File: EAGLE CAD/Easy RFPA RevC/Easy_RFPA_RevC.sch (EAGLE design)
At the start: 305 parts, among them IC1 LM741D, IC2 LM741D, IC3 LM393D, IC5 74AHC1G00DBV, IC6 74LS74D, IC7 74AHC1G86DBV, J101 COAX112640BNC_EDGE, J102 COAX112640BNC_EDGE, J301 COAX112640BNC_EDGE, J302 COAX112640BNC_EDGE, J401 HDR_2X1282836-1282836-1, J402 KK_PCFAN, Q1 IRF630, Q101 IRF520N, Q102 IRF630, Q2 MOSFET_NBSS123SOT23, Q201 IRF630, Q202 IRF630, Q3 NPNMMBT3904SOT23_BEC, Q301 MOSFET_NBSS123SOT23, Q302 PNPSOT23_BEC, Q303 NPNMMBT3904SOT23_BEC, Q4 PNPSOT23_BEC, T1 HP1_TRAFO, T102 HP4_TRAFO, U1 OPAMP_QUADTLV274IDSOIC14, U302 OPAMP_QUADTLV274IDSOIC14, U401 LDO_3TERMMC78M12CTGTO220_VERT, U402 LDO_3TERMMC78M05CTGTO220_VERT, X1 1-227161-0, X2 1-227161-0, X3 1-227161-0, X4 1-227161-0, X402 HEATSINK_OMNI_DUALOMNI-UNI-30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

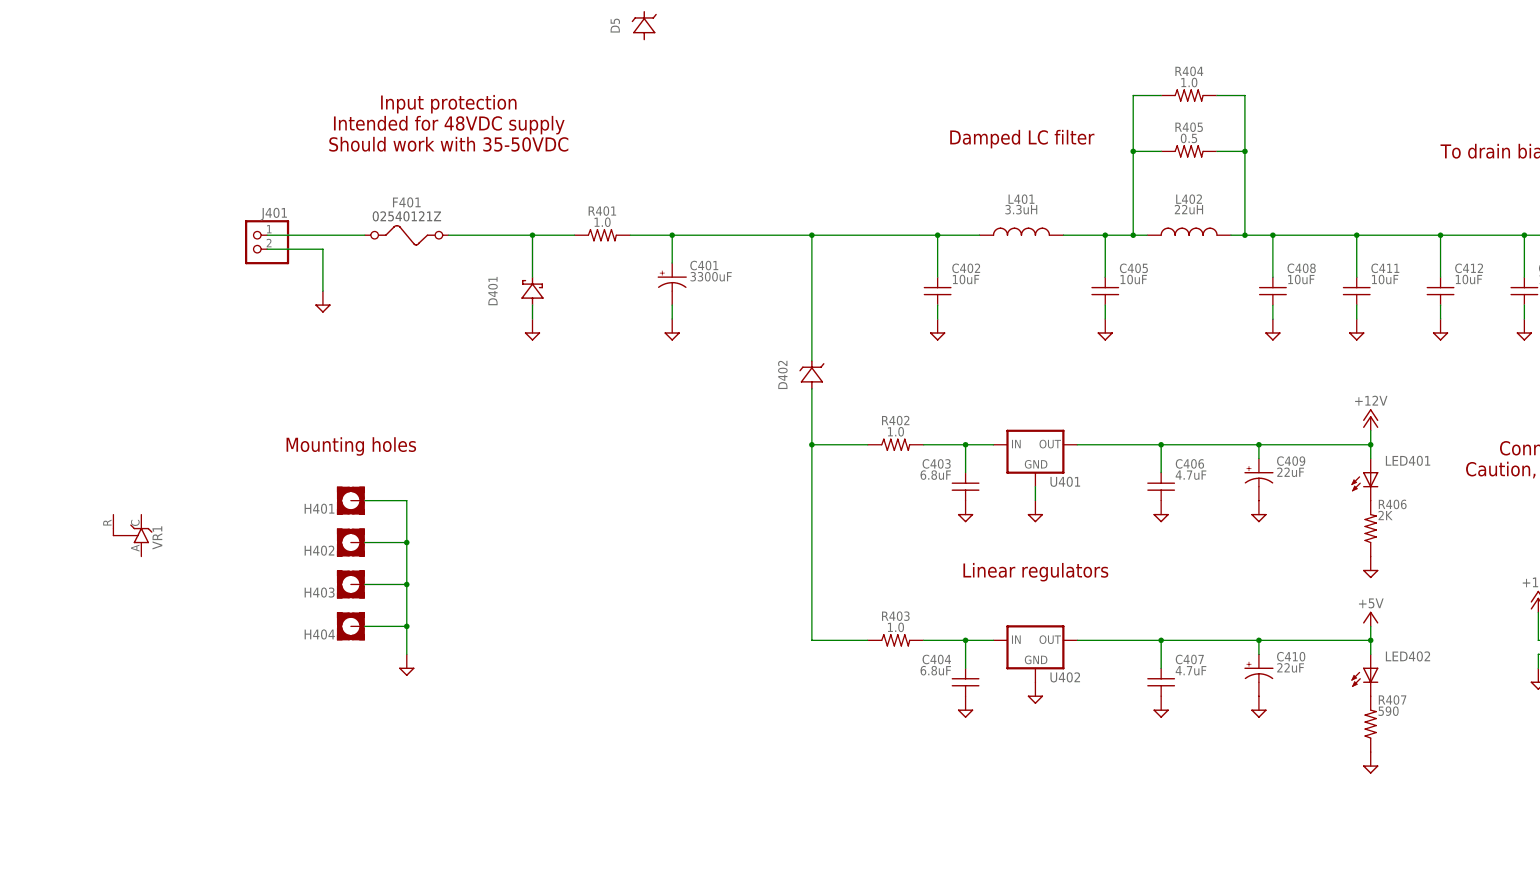
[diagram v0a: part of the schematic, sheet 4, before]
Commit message: Move connectors/LEDs/buttons to west edge
Aiming to have these poke through a panel.
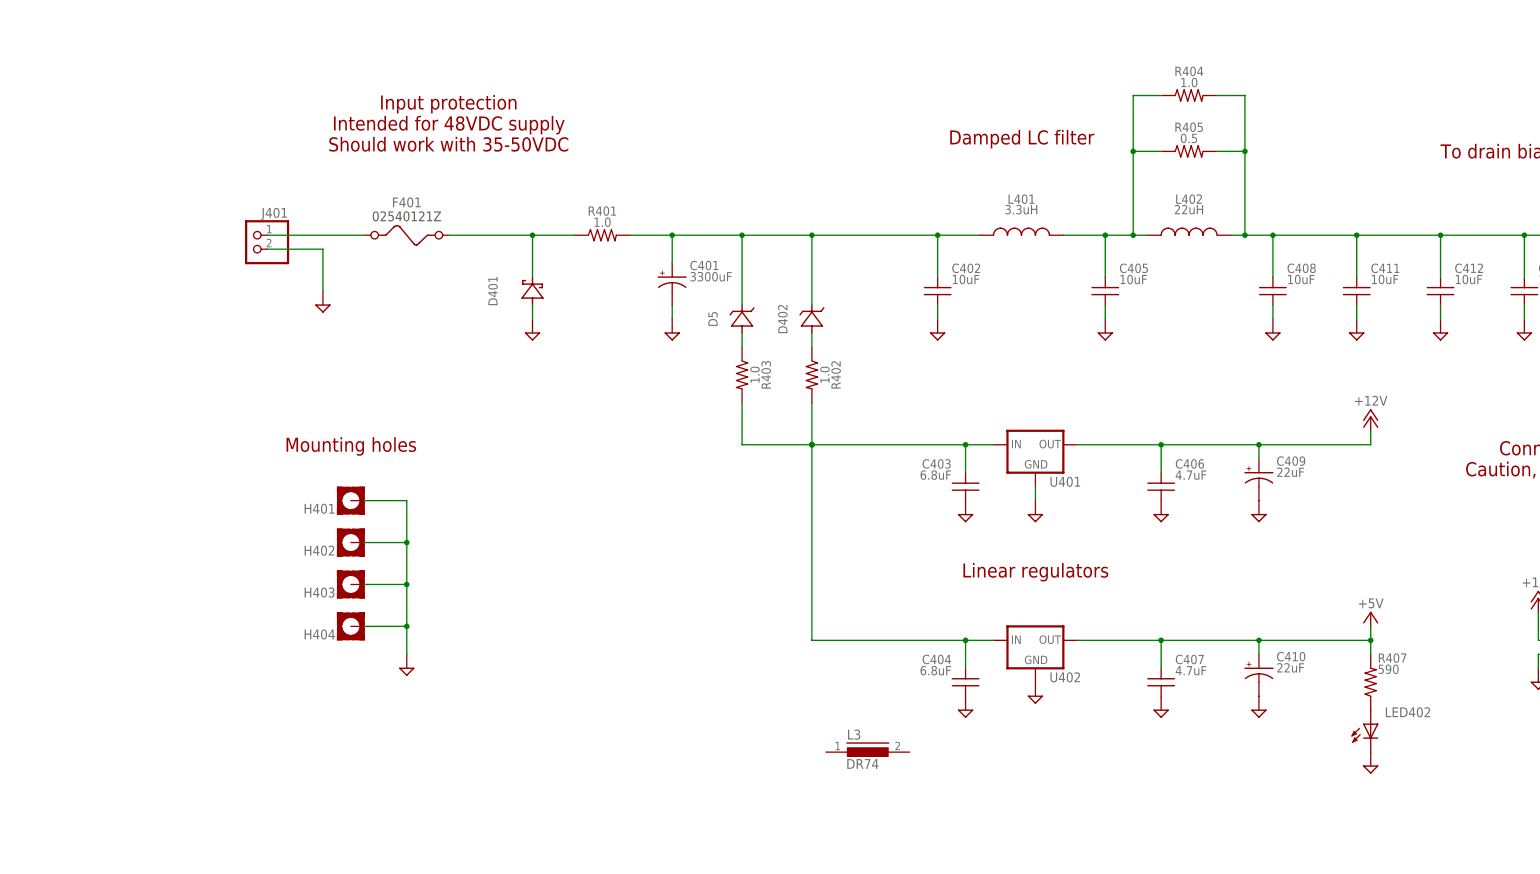
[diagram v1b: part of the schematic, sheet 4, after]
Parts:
- removed C114, C115, C211, C212: 10nF, MDT_C:CGEN0805_IPC
- removed J101, J102, J301, J302: COAX112640BNC_EDGE, MDT_CON:COAX112640BNC_EDGE
- removed LED401: LEDHLMP-3962-F0002T1_3/4, MDT_Diode:LEDHLMP-3962-F0002T1_3/4
- removed R130, R131, R229, R230, R24: 1K, MDT_R:R90GEN0805_IPC
- removed R406: 2K, MDT_R:RGEN0805_IPC
- removed S1, S2: (no value), switch-omron:10-XX
- removed TP14, TP15, TP16, TP17, TP24: PROBE_TPTP_5MM, MDT_CON:PROBE_TPTP_5MM
- removed VR1: (no value), v-reg:TL431CLP
- added L1: (no value), MDT_L:LDR74
- added L3: DR74, inductors:DR74
- added SW1, SW2: SPST_NO_TACT_RA431256083716431256083716, MDT_SWITCH:SPST_NO_TACT_RA431256083716431256083716
- C8: value 10nF -> 22nF; device MDT_C:CGEN0805_IPC -> MDT_C:CC-22N-250V-5%-1206-NP0C1206; BOM (none) -> EXCLUDE; VOLTAGE 50V -> (none)
- LED1, LED2: value LEDHLMP-3401-E0002T1_3/4 -> LEDT1_3/4_RA; device MDT_Diode:LEDHLMP-3401-E0002T1_3/4 -> MDT_Diode:LEDT1_3/4_RA
- LED402: value LEDHLMP-3962-F0002T1_3/4 -> LEDT1_3/4_RA; device MDT_Diode:LEDHLMP-3962-F0002T1_3/4 -> MDT_Diode:LEDT1_3/4_RA
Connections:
- removed net AN6: C115.1, R131.2, TP15.1
- removed net AP6: C114.1, R130.2, TP14.1
- removed net BN6: C212.1, R230.2, TP17.1
- removed net BP6: C211.1, R229.2, TP16.1
- removed net N$49: C404.1, R403.2, U402.IN
- removed net S1_BP6: C8.1, R24.2, TP24.1
- net !FAULT: now also SW1.P1; no longer S2.P, S2.P1
- net +12V: no longer LED401.A
- net +5V: now also R407.1, SW2.P1; no longer LED402.A, S1.P, S1.P1
- net AN5: no longer R131.1
- net AP5: no longer R130.1
- net BN5: no longer R230.1
- net BP5: no longer R229.1
- net GND: now also LED402.C, SW1.G1, SW1.G2, SW1.S1, SW2.G1, SW2.G2; no longer C114.2, C115.2, C211.2, C212.2, C8.2, J101.GND1, J102.GND1, J302.GND1, R406.2, R407.2, S2.S, S2.S1, TP14.GND1, TP15.GND1, TP16.GND1, TP17.GND1, TP24.GND1
- net N$20: no longer J301.1
- net N$21: no longer J301.GND1
- net N$28: now also D5.A1; no longer D402.A1, R402.1
- net N$31: no longer J102.1
- net N$32: now also D402.A1, R402.1; no longer LED401.C, R406.1
- net N$33: now also LED402.A, R407.2; no longer LED402.C, R407.1
- net N$43: now also C404.1, R403.2, U402.IN
- net N$46: now also D5.C1
- net N$53: no longer J302.1
- net N$69: no longer J101.1
- net RESET: now also SW2.S1; no longer S1.S, S1.S1
- net S1_BP5: no longer R24.1
- net S2_DP: now also C8.2, L1.1
- net VB: now also C8.1, L1.2
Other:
- moved on the sheet: C4, C8, D402, D5, LED402, R402, R403, R407, R8

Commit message: Try and keep area under 30 square inches
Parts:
- removed L3: DR74, inductors:DR74
- removed X3: 1-227161-0, con-coax:1-227161-0
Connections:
- net N$20: no longer X3.1
- net N$21: no longer X3.2
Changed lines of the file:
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@@
 <part name="X1" library="con-coax" deviceset="?227161*" device="1-" technology="-0"/>
 <part name="X2" library="con-coax" deviceset="?227161*" device="1-" technology="-0"/>
-<part name="X3" library="con-coax" deviceset="?227161*" device="1-" technology="-0"/>
 <part name="X4" library="con-coax" deviceset="?227161*" device="1-" technology="-0"/>
 <part name="SUPPLY6" library="supply2" deviceset="GND" device=""/>
@@
 <variant name="IRF630_200W"/>
 </part>
-<part name="L3" library="inductors" deviceset="DR74" device=""/>
 <part name="C8" library="MDT_C" deviceset="C" device="C1206" technology="C-22N-250V-5%-1206-NP0" value="22nF">
 <attribute name="BOM" value="EXCLUDE"/>
 </part>
 <part name="D5" library="MDT_Diode" deviceset="D-ZENER" device="DO15-12" technology="1N5355B-TP" value="D-ZENER1N5355B-TPDO15-12"/>
+<part name="X3" library="MDT_HEATSINK" deviceset="THERMALPAD_TO220" device="" technology="DC0011/15-TI900-0.12-0"/>
+<part name="X5" library="MDT_HEATSINK" deviceset="HEATSINK_CLIP" device="" technology="OMNI-220C"/>
 </parts>
 <sheets>
@@
 <instance part="U1" gate="C" x="111.76" y="83.82"/>
 <instance part="U1" gate="P" x="200.66" y="76.2"/>
-<instance part="X3" gate="G$1" x="66.04" y="246.38"/>
 <instance part="SUPPLY42" gate="GND" x="93.98" y="78.74" smashed="yes"/>
 <instance part="R44" gate="G$1" x="317.5" y="182.88"/>
@@
 <segment>
 <wire x1="93.98" y1="233.68" x2="88.9" y2="233.68" width="0.1524" layer="91"/>
-<wire x1="88.9" y1="233.68" x2="73.66" y2="233.68" width="0.1524" layer="91"/>
-<wire x1="68.58" y1="223.52" x2="73.66" y2="223.52" width="0.1524" layer="91"/>
-<wire x1="73.66" y1="223.52" x2="73.66" y2="233.68" width="0.1524" layer="91"/>
 <pinref part="JP301" gate="G$1" pin="2"/>
 <wire x1="81.28" y1="223.52" x2="88.9" y2="223.52" width="0.1524" layer="91"/>
 <wire x1="88.9" y1="223.52" x2="88.9" y2="233.68" width="0.1524" layer="91"/>
-<junction x="88.9" y="233.68"/>
 <pinref part="R302" gate="G$1" pin="1"/>
-<pinref part="X3" gate="G$1" pin="1"/>
-<wire x1="68.58" y1="246.38" x2="73.66" y2="246.38" width="0.1524" layer="91"/>
-<wire x1="73.66" y1="246.38" x2="73.66" y2="233.68" width="0.1524" layer="91"/>
-<junction x="73.66" y="233.68"/>
 </segment>
 </net>
@@
 <wire x1="93.98" y1="213.36" x2="88.9" y2="213.36" width="0.1524" layer="91"/>
 <pinref part="JP301" gate="G$1" pin="1"/>
-<wire x1="88.9" y1="213.36" x2="73.66" y2="213.36" width="0.1524" layer="91"/>
-<wire x1="73.66" y1="213.36" x2="73.66" y2="220.98" width="0.1524" layer="91"/>
-<wire x1="73.66" y1="220.98" x2="71.12" y2="220.98" width="0.1524" layer="91"/>
-<wire x1="71.12" y1="220.98" x2="68.58" y2="220.98" width="0.1524" layer="91"/>
 <wire x1="81.28" y1="220.98" x2="88.9" y2="220.98" width="0.1524" layer="91"/>
 <wire x1="88.9" y1="220.98" x2="88.9" y2="213.36" width="0.1524" layer="91"/>
-<junction x="88.9" y="213.36"/>
 <pinref part="R303" gate="G$1" pin="1"/>
-<pinref part="X3" gate="G$1" pin="2"/>
-<wire x1="68.58" y1="243.84" x2="71.12" y2="243.84" width="0.1524" layer="91"/>
-<wire x1="71.12" y1="243.84" x2="71.12" y2="220.98" width="0.1524" layer="91"/>
-<junction x="71.12" y="220.98"/>
 </segment>
 </net>
@@
 <instance part="FRAME1" gate="G$1" x="0" y="0"/>
 <instance part="FRAME1" gate="G$2" x="325.12" y="0"/>
-<instance part="L3" gate="G$1" x="167.64" y="81.28"/>
 <instance part="D5" gate="G$1" x="144.78" y="160.02" rot="R90"/>
+<instance part="X3" gate="G$1" x="350.52" y="78.74"/>
+<instance part="X5" gate="G$1" x="365.76" y="73.66"/>
 </instances>
 <busses>

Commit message: Slip around S2 layout
Fits better with surroundings
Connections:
- removed net S1_DN: C1.1, T1.F3
- new net N$49: C1.1, T1.S6
- net VB: now also T1.F3; no longer T1.S6
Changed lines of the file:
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@@
 </segment>
 <segment>
-<wire x1="63.5" y1="152.4" x2="63.5" y2="144.78" width="0.1524" layer="91"/>
-<pinref part="T1" gate="G$1" pin="S6"/>
-<wire x1="63.5" y1="152.4" x2="48.26" y2="152.4" width="0.1524" layer="91"/>
 <label x="48.26" y="152.4" size="1.778" layer="95"/>
+<pinref part="T1" gate="G$1" pin="F3"/>
+<wire x1="53.34" y1="152.4" x2="48.26" y2="152.4" width="0.1524" layer="91"/>
+<wire x1="78.74" y1="114.3" x2="78.74" y2="96.52" width="0.1524" layer="91"/>
+<wire x1="53.34" y1="96.52" x2="78.74" y2="96.52" width="0.1524" layer="91"/>
+<wire x1="53.34" y1="152.4" x2="53.34" y2="96.52" width="0.1524" layer="91"/>
 </segment>
 </net>
@@
 </segment>
 </net>
-<net name="S1_DN" class="1">
-<segment>
-<pinref part="T1" gate="G$1" pin="F3"/>
-<wire x1="78.74" y1="114.3" x2="78.74" y2="96.52" width="0.1524" layer="91"/>
-<pinref part="C1" gate="G$1" pin="1"/>
-<wire x1="48.26" y1="96.52" x2="78.74" y2="96.52" width="0.1524" layer="91"/>
-</segment>
-</net>
 <net name="T1_P2" class="3">
 <segment>
@@
 </segment>
 </net>
+<net name="N$49" class="3">
+<segment>
+<wire x1="63.5" y1="152.4" x2="63.5" y2="149.86" width="0.1524" layer="91"/>
+<pinref part="T1" gate="G$1" pin="S6"/>
+<pinref part="C1" gate="G$1" pin="1"/>
+<wire x1="63.5" y1="149.86" x2="63.5" y2="144.78" width="0.1524" layer="91"/>
+<wire x1="48.26" y1="96.52" x2="50.8" y2="96.52" width="0.1524" layer="91"/>
+<wire x1="50.8" y1="96.52" x2="50.8" y2="149.86" width="0.1524" layer="91"/>
+<wire x1="50.8" y1="149.86" x2="63.5" y2="149.86" width="0.1524" layer="91"/>
+<junction x="63.5" y="149.86"/>
+</segment>
+</net>

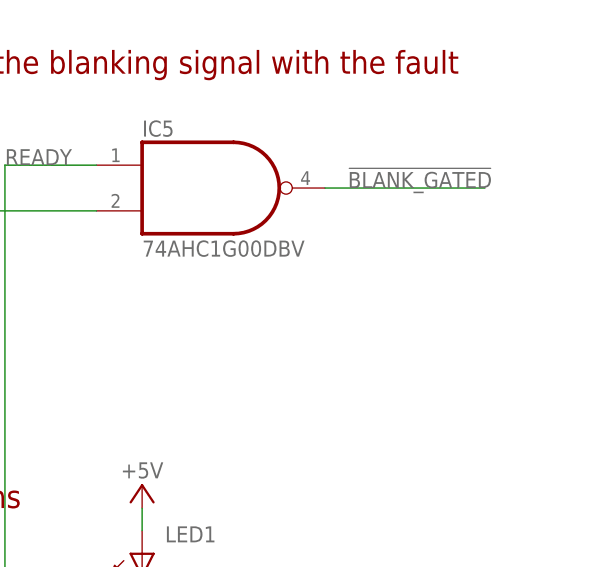
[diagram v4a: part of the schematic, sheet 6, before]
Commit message: cleaning up revC
fixed all major DRC errors
returned all nets to default class
all airwires routed
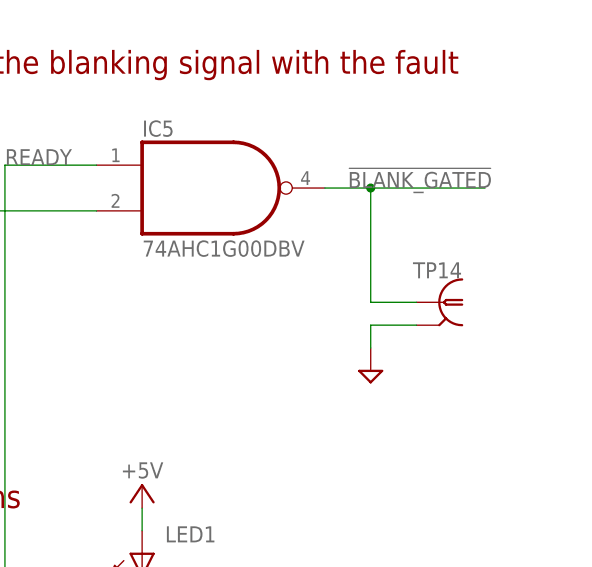
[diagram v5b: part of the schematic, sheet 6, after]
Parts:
- added TP14: PROBE_TPTP_5MM, MDT_CON:PROBE_TPTP_5MM
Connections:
- net !BLANK_GATED: now also TP14.1
- net GND: now also TP14.GND1
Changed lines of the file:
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@@
 <part name="X5" library="MDT_HEATSINK" deviceset="HEATSINK_CLIP" device="" technology="OMNI-220C"/>
 <part name="L1" library="MDT_L" deviceset="L" device="DR74"/>
+<part name="TP14" library="MDT_CON" deviceset="PROBE_TP" device="TP_5MM"/>
+<part name="SUPPLY51" library="supply2" deviceset="GND" device=""/>
 </parts>
 <sheets>
@@
 </segment>
 </net>
-<net name="VB_CT" class="2">
+<net name="VB_CT" class="0">
 <segment>
 <wire x1="350.52" y1="144.78" x2="350.52" y2="149.86" width="0.1524" layer="91"/>
@@
 </segment>
 </net>
-<net name="VB" class="3">
+<net name="VB" class="0">
 <segment>
 <wire x1="307.34" y1="218.44" x2="302.26" y2="218.44" width="0.1524" layer="91"/>
@@
 </segment>
 </net>
-<net name="S2_DP" class="2">
+<net name="S2_DP" class="0">
 <segment>
 <pinref part="C1" gate="G$1" pin="2"/>
@@
 </segment>
 </net>
-<net name="T1_P2" class="3">
+<net name="T1_P2" class="0">
 <segment>
 <wire x1="68.58" y1="114.3" x2="68.58" y2="109.22" width="0.1524" layer="91"/>
@@
 </segment>
 </net>
-<net name="N$49" class="3">
+<net name="N$49" class="0">
 <segment>
 <wire x1="63.5" y1="152.4" x2="63.5" y2="149.86" width="0.1524" layer="91"/>
@@
 </segment>
 </net>
-<net name="N$47" class="2">
+<net name="N$47" class="0">
 <segment>
 <wire x1="203.2" y1="175.26" x2="210.82" y2="175.26" width="0.1524" layer="91"/>
@@
 </segment>
 </net>
-<net name="VB" class="3">
+<net name="VB" class="0">
 <segment>
 <wire x1="231.14" y1="190.5" x2="236.22" y2="190.5" width="0.1524" layer="91"/>
@@
 </segment>
 </net>
-<net name="S2_DP" class="2">
+<net name="S2_DP" class="0">
 <segment>
 <pinref part="C7" gate="G$1" pin="2"/>
@@
 </segment>
 </net>
-<net name="VB" class="3">
+<net name="VB" class="0">
 <segment>
 <wire x1="284.48" y1="132.08" x2="284.48" y2="134.62" width="0.1524" layer="91"/>
@@
 <instance part="SUPPLY49" gate="GND" x="406.4" y="45.72" smashed="yes"/>
 <instance part="SUPPLY50" gate="GND" x="421.64" y="45.72" smashed="yes"/>
+<instance part="TP14" gate="G$1" x="563.88" y="129.54" rot="MR0"/>
+<instance part="SUPPLY51" gate="GND" x="556.26" y="121.92" smashed="yes"/>
 </instances>
 <busses>
@@
 <wire x1="421.64" y1="50.8" x2="421.64" y2="48.26" width="0.1524" layer="91"/>
 </segment>
+<segment>
+<pinref part="TP14" gate="G$1" pin="GND1"/>
+<wire x1="561.34" y1="127" x2="556.26" y2="127" width="0.1524" layer="91"/>
+<wire x1="556.26" y1="127" x2="556.26" y2="124.46" width="0.1524" layer="91"/>
+<pinref part="SUPPLY51" gate="GND" pin="GND"/>
+</segment>
 </net>
 <net name="N$3" class="0">
@@
 <net name="!BLANK_GATED" class="0">
 <segment>
-<wire x1="551.18" y1="142.24" x2="568.96" y2="142.24" width="0.1524" layer="91"/>
+<wire x1="551.18" y1="142.24" x2="556.26" y2="142.24" width="0.1524" layer="91"/>
 <label x="553.72" y="142.24" size="1.778" layer="95"/>
 <pinref part="IC5" gate="A" pin="O"/>
+<pinref part="TP14" gate="G$1" pin="1"/>
+<wire x1="556.26" y1="142.24" x2="568.96" y2="142.24" width="0.1524" layer="91"/>
+<wire x1="561.34" y1="129.54" x2="556.26" y2="129.54" width="0.1524" layer="91"/>
+<wire x1="556.26" y1="129.54" x2="556.26" y2="142.24" width="0.1524" layer="91"/>
+<junction x="556.26" y="142.24"/>
 </segment>
 </net>

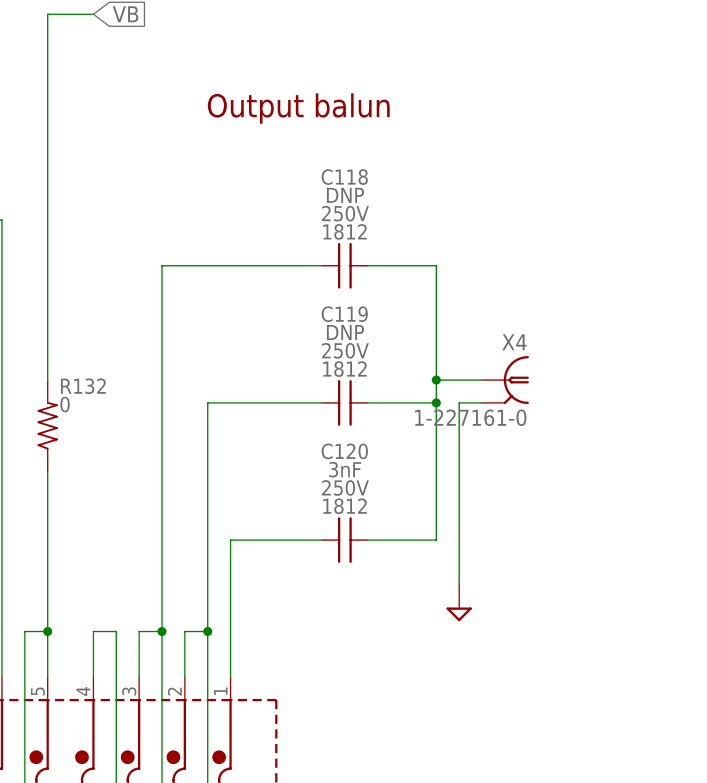
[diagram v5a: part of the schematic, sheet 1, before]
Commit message: Output balun section
To save space, remove C119 and C120, replace with 1206 resistors instead to select turns ratio
Put all drain bias inductors back on top side
Add keepouts to inductor packages
Move R44-47 to centerline, away from FETs
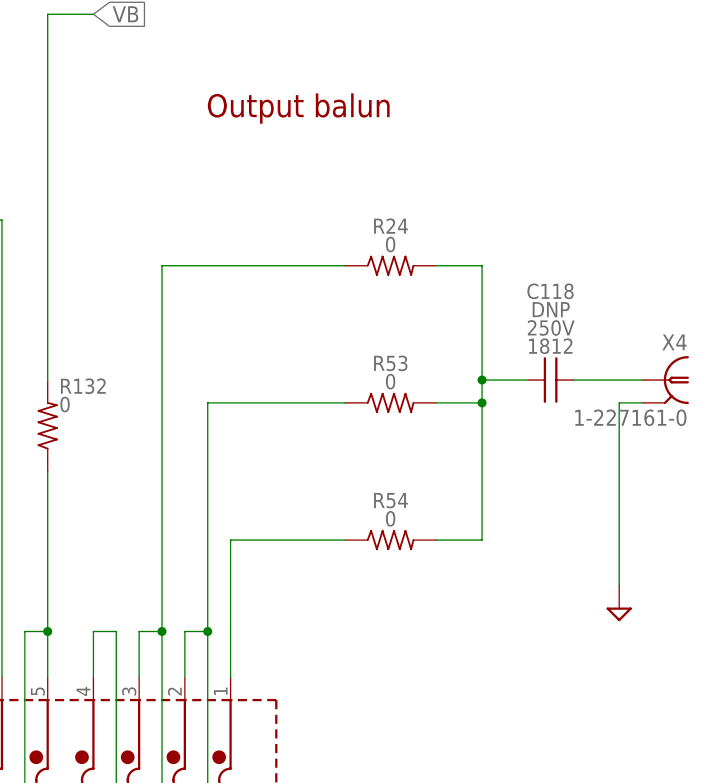
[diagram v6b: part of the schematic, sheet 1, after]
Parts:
- removed C119: DNP, MDT_C:CGENC1812
- removed C120: 3nF, MDT_C:CGENC1812
- added R24, R53, R54: 0, MDT_R:R90GEN1206_IPC
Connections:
- new net N$85: C118.1, R24.2, R53.2, R54.2
- net N$29: now also R53.1; no longer C119.1
- net N$30: now also R54.1; no longer C120.1
- net N$31: no longer C119.2, C120.2
- net N$52: now also R24.1; no longer C118.1
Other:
- moved on the sheet: C118, X4
